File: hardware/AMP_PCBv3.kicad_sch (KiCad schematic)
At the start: 50 parts, among them CN10 Male_R2, CN7 Male_L1, J1 Input_PWR, J3 LED_Header, J4 VESC_PPM, J5 VESC_COMM, J6 STEERING, M2 Fan_PC_3pin, M3 Fan_PC_3pin, M4 Fan_PC_3pin, M5 Fan_PC_3pin, Q1 DMN2310U, Q2 DMN2310U, Q3 DMN2310U, Q4 DMN2310U, U1 TPS56624x, U2 RFM95W-915S2

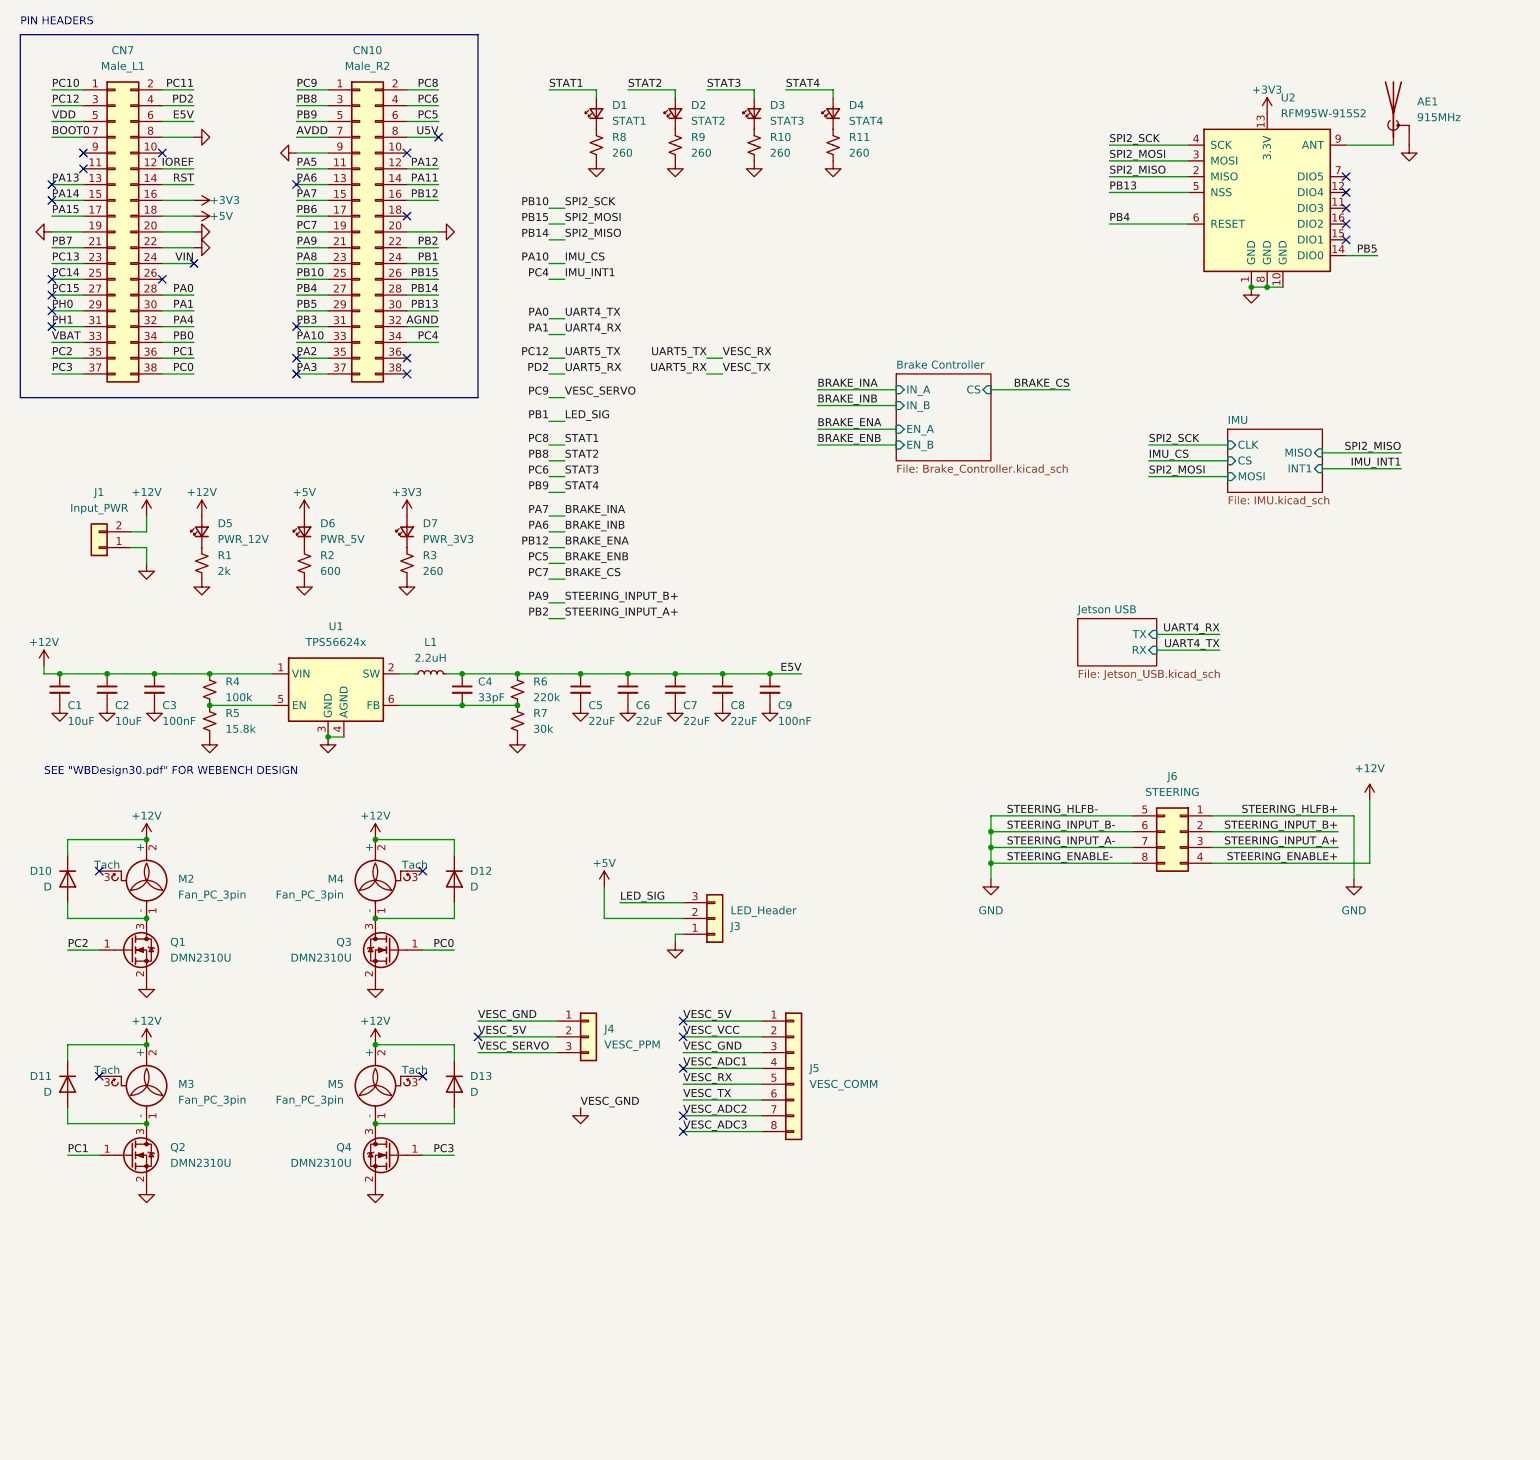
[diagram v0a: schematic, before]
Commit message: Add level shifters
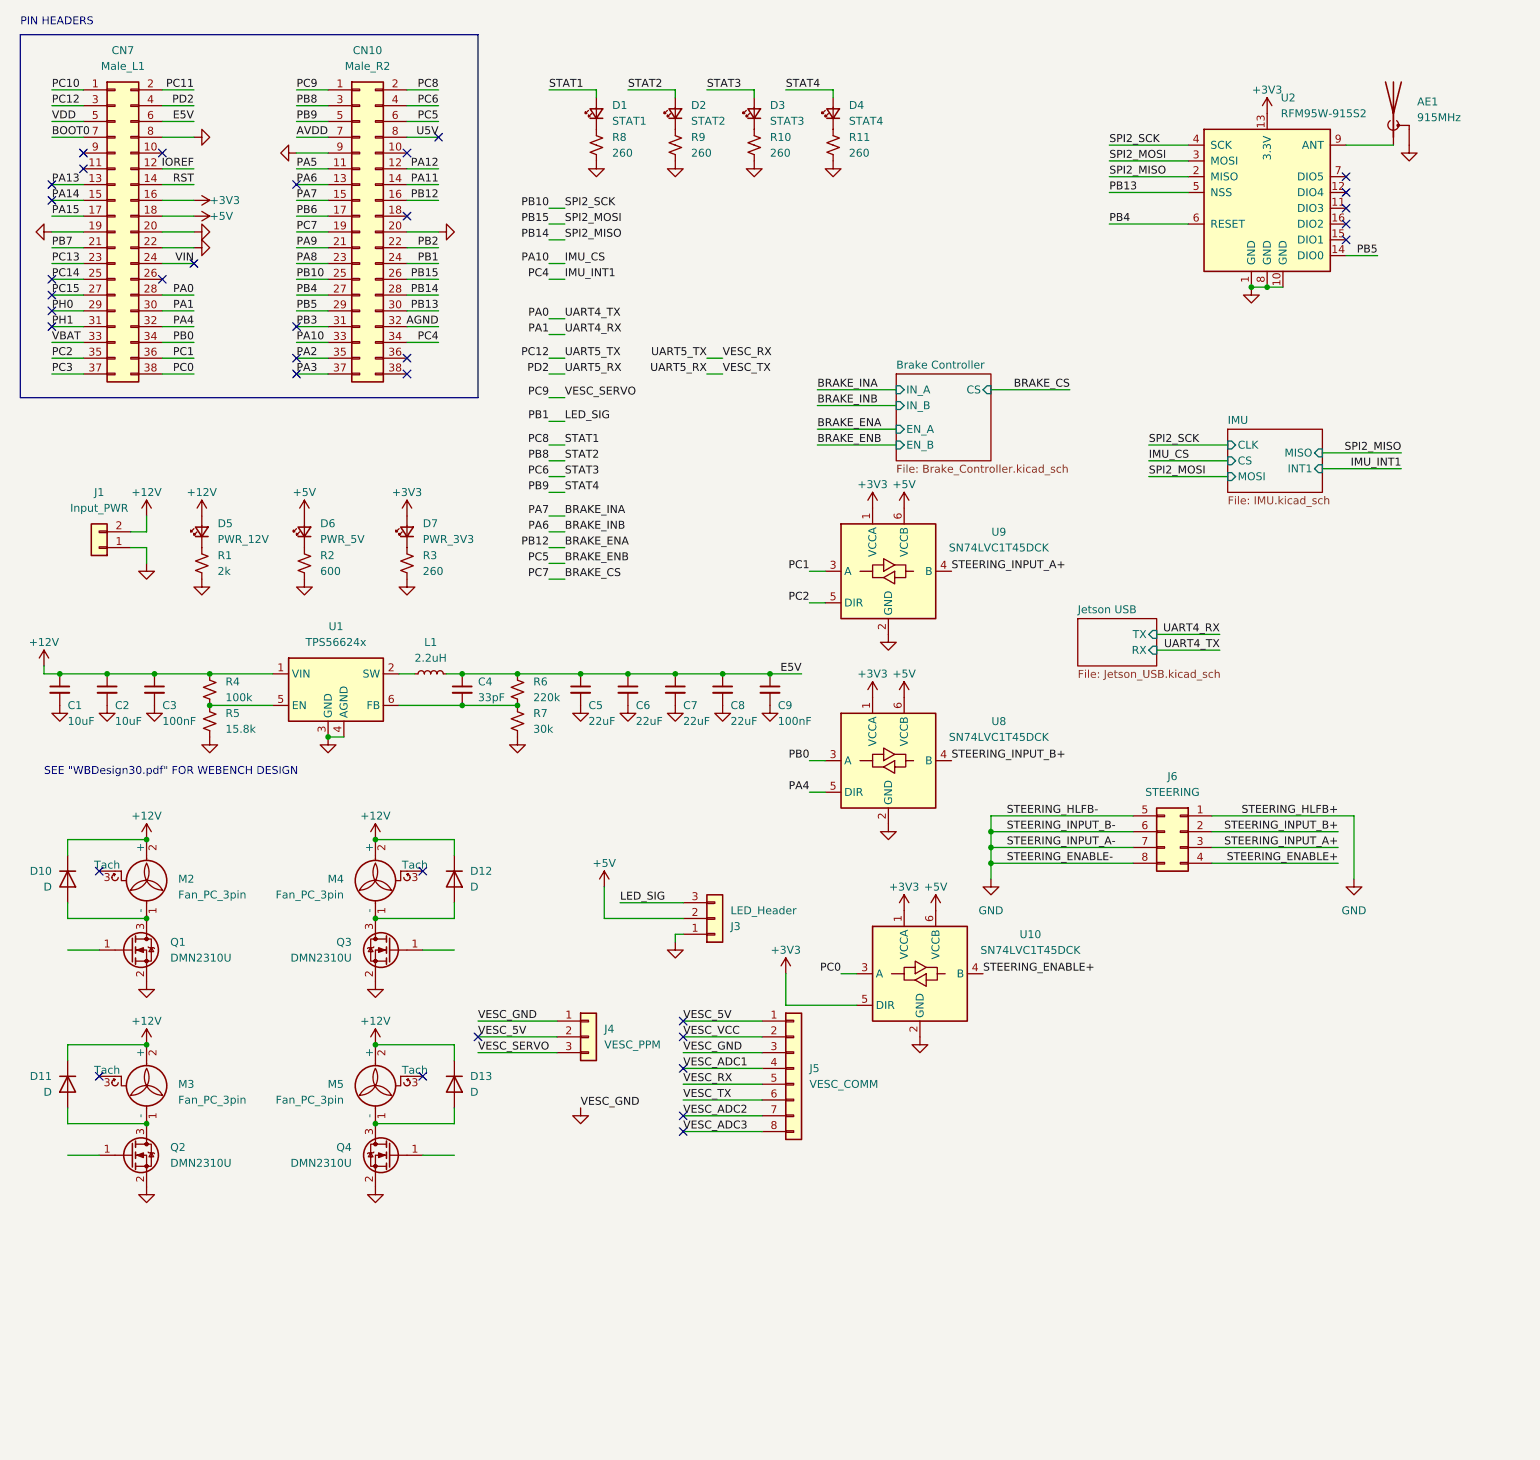
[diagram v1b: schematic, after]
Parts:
- added U10, U8, U9: SN74LVC1T45DCK, Package_TO_SOT_SMD:SOT-363_SC-70-6, symbol Logic_LevelTranslator:SN74LVC1T45DCK
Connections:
- net +12V: no longer J6.4 (Pin_4)
- net +3V3: now also U10.1 (VCCA), U10.5 (DIR), U8.1 (VCCA), U9.1 (VCCA)
- net +5V: now also U10.6 (VCCB), U8.6 (VCCB), U9.6 (VCCB)
- net GND: now also U10.2 (GND), U8.2 (GND), U9.2 (GND)
- net PA4: now also U8.5 (DIR)
- net PA9: no longer J6.2 (Pin_2)
- net PB0: now also U8.3 (A)
- net PB2: no longer J6.3 (Pin_3)
- net PC0: now also U10.3 (A); no longer Q3.1 (G)
- net PC1: now also U9.3 (A); no longer Q2.1 (G)
- net PC2: now also U9.5 (DIR); no longer Q1.1 (G)
- net PC3: no longer Q4.1 (G)
- new net STEERING_ENABLE+: J6.4 (Pin_4), U10.4 (B)
- new net STEERING_INPUT_A+: J6.3 (Pin_3), U9.4 (B)
- new net STEERING_INPUT_B+: J6.2 (Pin_2), U8.4 (B)

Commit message: Place and route
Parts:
- removed C3, C9: 100nF, Capacitor_SMD:C_0805_2012Metric_Pad1.18x1.45mm_HandSolder, symbol Device:C_Small
- removed C8: 22uF, Capacitor_SMD:C_0805_2012Metric_Pad1.18x1.45mm_HandSolder, symbol Device:C_Small
- removed U1: TPS56624x, Package_TO_SOT_SMD:SOT-563, symbol AMP_Custom:TPS56624x
- added U1: AP64500, Package_SO:Diodes_SO-8EP, symbol AMP_Custom:AP64500
- C2: value 10uF -> 2.7nF
- C4: value 33pF -> 100nF
- L1: value 2.2uH -> 3.6uH; footprint Inductor_SMD:L_Vishay_IHLP-2525 -> Inductor_SMD:L_Changjiang_FNR8040S
- R4: value 100k -> 200k
- R6: value 220k -> 115k
- R7: value 30k -> 22.1k
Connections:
- net BRAKE_ENB is gone; now on net BRAKE_CS: CN10.6 (Pin_6)
- net +12V: now also U1.2 (VIN), U1.3 (EN); no longer C2.1, R4.1
- net +5V: no longer J3.2 (Pin_2)
- net BRAKE_CS: no longer CN10.19 (Pin_19)
- net BRAKE_INA: now also CN10.2 (Pin_2); no longer CN10.15 (Pin_15)
- net BRAKE_INB: now also CN10.4 (Pin_4); no longer CN10.13 (Pin_13)
- net E5V: now also J3.2 (Pin_2); no longer C4.1
- net GND: now also R4.1, U1.7 (GND), U1.9 (GND); no longer R5.2
- net PA11: now also D3.2 (A)
- net PA12: now also D1.2 (A)
- net PA15: now also Q1.1 (G)
- net PA5: now also D2.2 (A)
- net PB7: now also Q2.1 (G)
- net PC10: now also Q4.1 (G)
- net PC11: now also Q3.1 (G)
- net at R6.2, R7.1: now also U1.5 (FB); no longer C4.2
- net at L1.1: now also C4.2, U1.8 (SW)
- net at R5.1: now also C2.1; no longer R4.2
- net BRAKE_ENA renamed PB12
- net PB12: now also D4.2 (A)
- net PB8 renamed BRAKE_SEL0
- net BRAKE_SEL0: no longer D2.2 (A)
- net PB9 renamed BRAKE_PWM
- net BRAKE_PWM: no longer D4.2 (A)
- removed net PC6: CN10.4 (Pin_4), D3.2 (A)
- removed net PC8: CN10.2 (Pin_2), D1.2 (A)
- new net: R5.2, U1.6 (COMP)
- new net: R4.2, U1.4 (RT/CLK)
- new net: C4.1, U1.1 (BST)
- new net PA6: CN10.13 (Pin_13)
- new net PA7: CN10.15 (Pin_15)
- new net PC7: CN10.19 (Pin_19)
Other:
- sheet Brake Controller ports: added PWM, SEL0; removed EN_A, EN_B
- note removed: "SEE "WBDesign30.pdf" FOR WEBENCH DESIGN"
- moved on the sheet: C4, C5, C6, L1, R6, R7

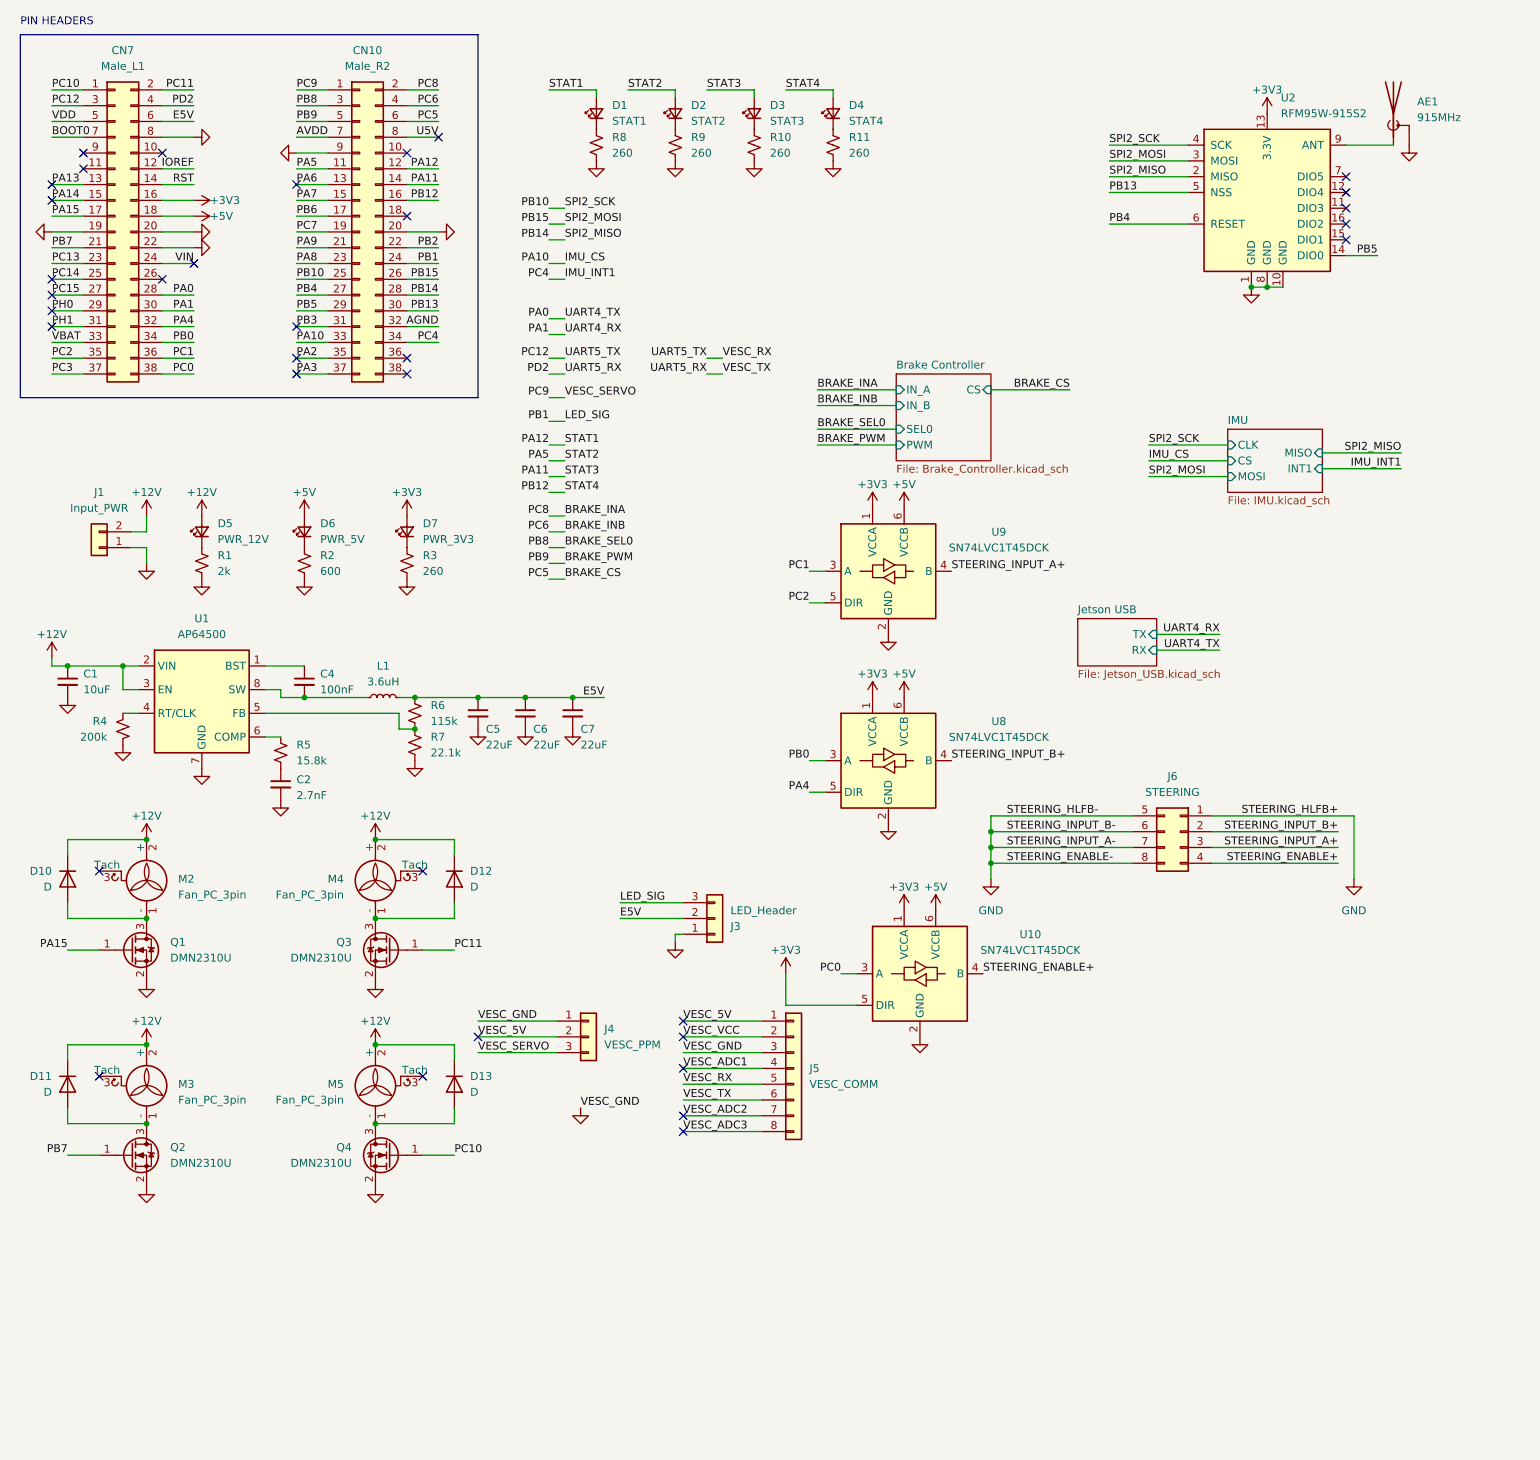
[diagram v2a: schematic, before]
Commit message: Add level shifter for LEDs
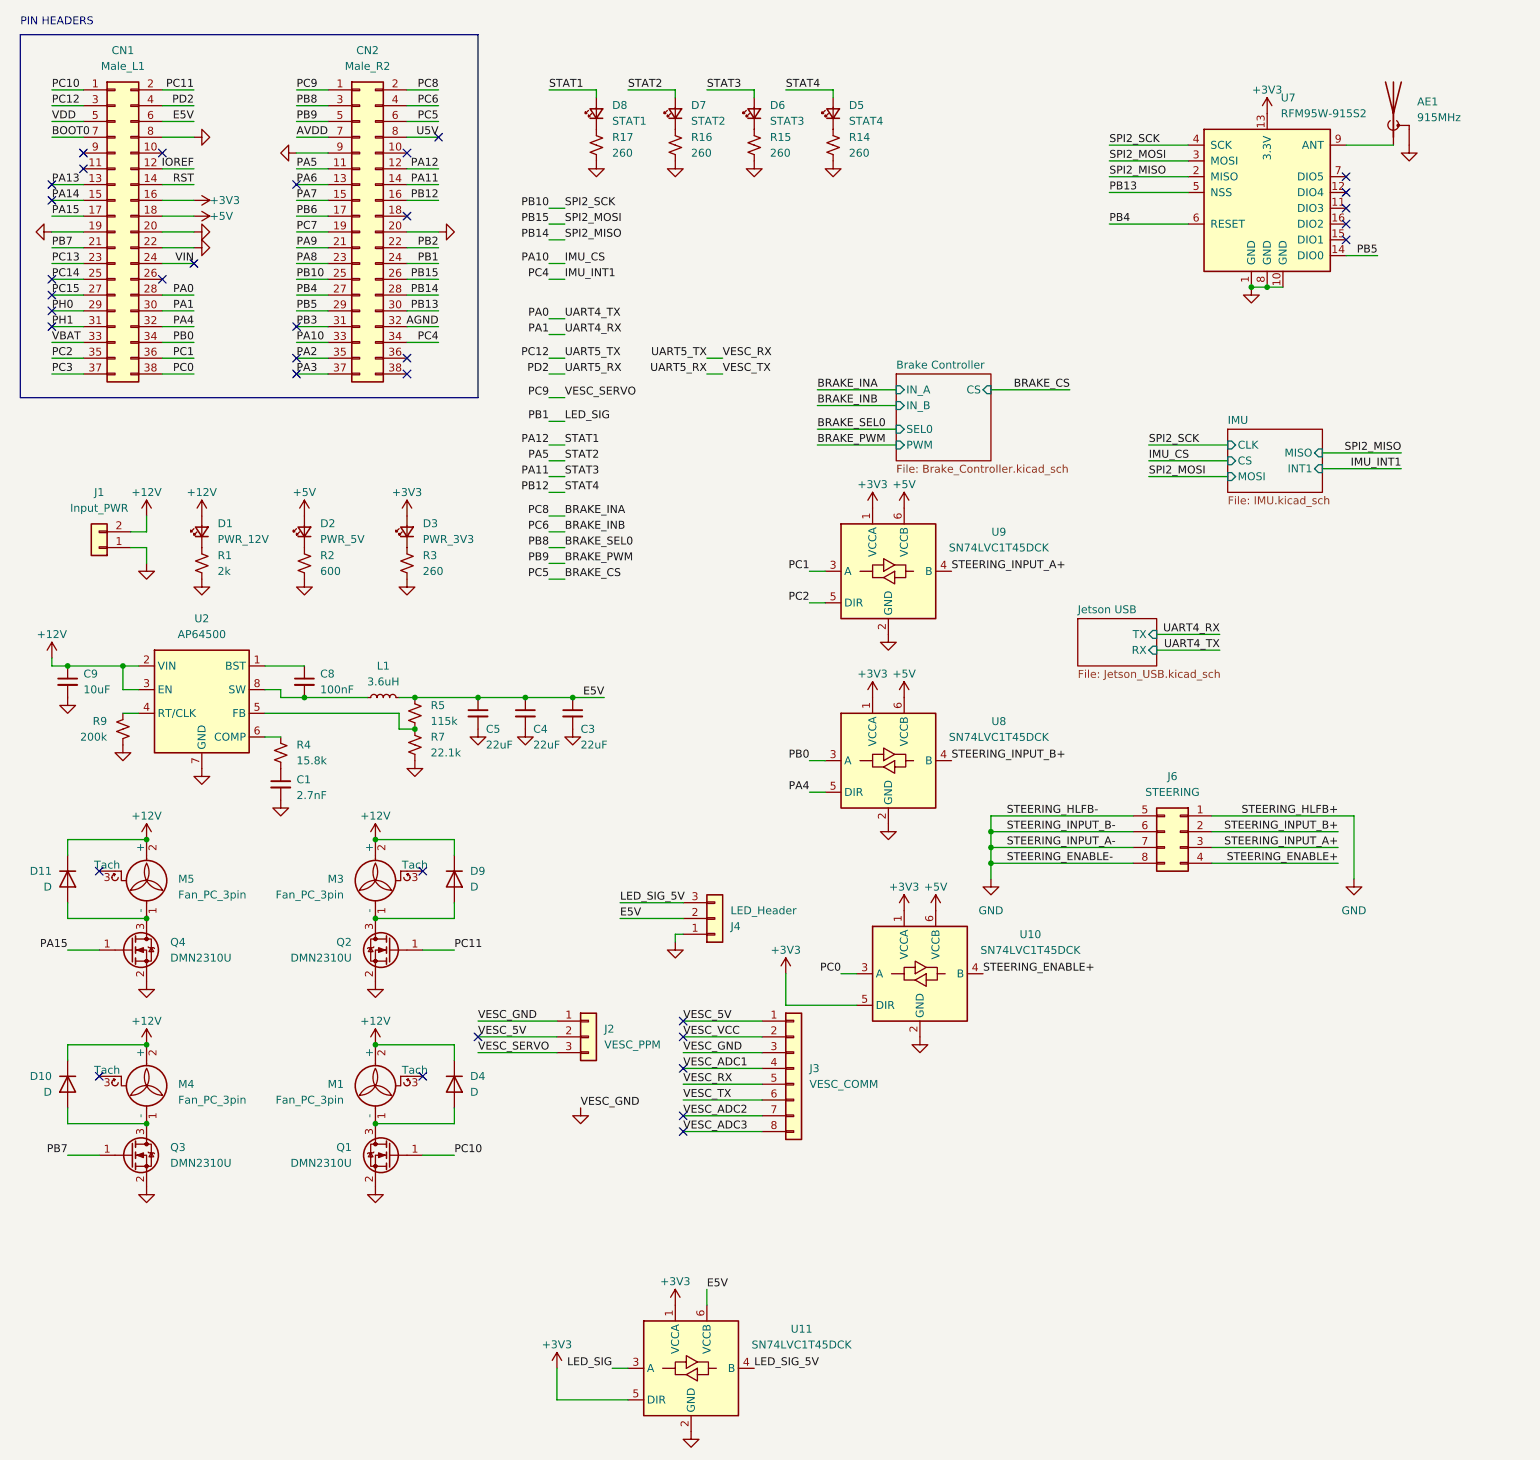
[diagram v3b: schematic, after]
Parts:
- added U11: SN74LVC1T45DCK, Package_TO_SOT_SMD:SOT-363_SC-70-6, symbol Logic_LevelTranslator:SN74LVC1T45DCK
- renumbered C2 to C1, C7 to C3, C6 to C4, C4 to C8, C1 to C9, CN7 to CN1, CN10 to CN2, D5 to D1, D11 to D10, D10 to D11, D6 to D2, D7 to D3, D13 to D4, D4 to D5, D3 to D6, D2 to D7, D1 to D8, D12 to D9, J4 to J2, J5 to J3, J3 to J4, M5 to M1, M4 to M3, M3 to M4, M2 to M5, Q4 to Q1, Q3 to Q2, Q2 to Q3, Q1 to Q4, R11 to R14, R10 to R15, R9 to R16, R8 to R17, R5 to R4, R6 to R5, R4 to R9, U1 to U2, U2 to U7
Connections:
- net +3V3: now also U11.1 (VCCA), U11.5 (DIR)
- net E5V: now also U11.6 (VCCB)
- net GND: now also U11.2 (GND)
- net LED_SIG: now also U11.3 (A); no longer J4.3 (Pin_3)
- new net LED_SIG_5V: J4.3 (Pin_3), U11.4 (B)
